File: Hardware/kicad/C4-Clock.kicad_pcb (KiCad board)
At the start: 2 copper layers, 99 x 99 mm, 29 parts, among them J1 Keypad, J2 Battery, J3 LCD1602, J4 Boost Module, J5 ICSP, K1 FINDER-36.11-5V, Q1 S9014, Q2 S9014, SW1 SW_SPST, SW2 SW_SPST, U1 ATmega328P-P, U2 AMS1117-5.0, U3 PCF8574A, U4 DS1302+, Y1 16MHz, Y2 32.768kHz

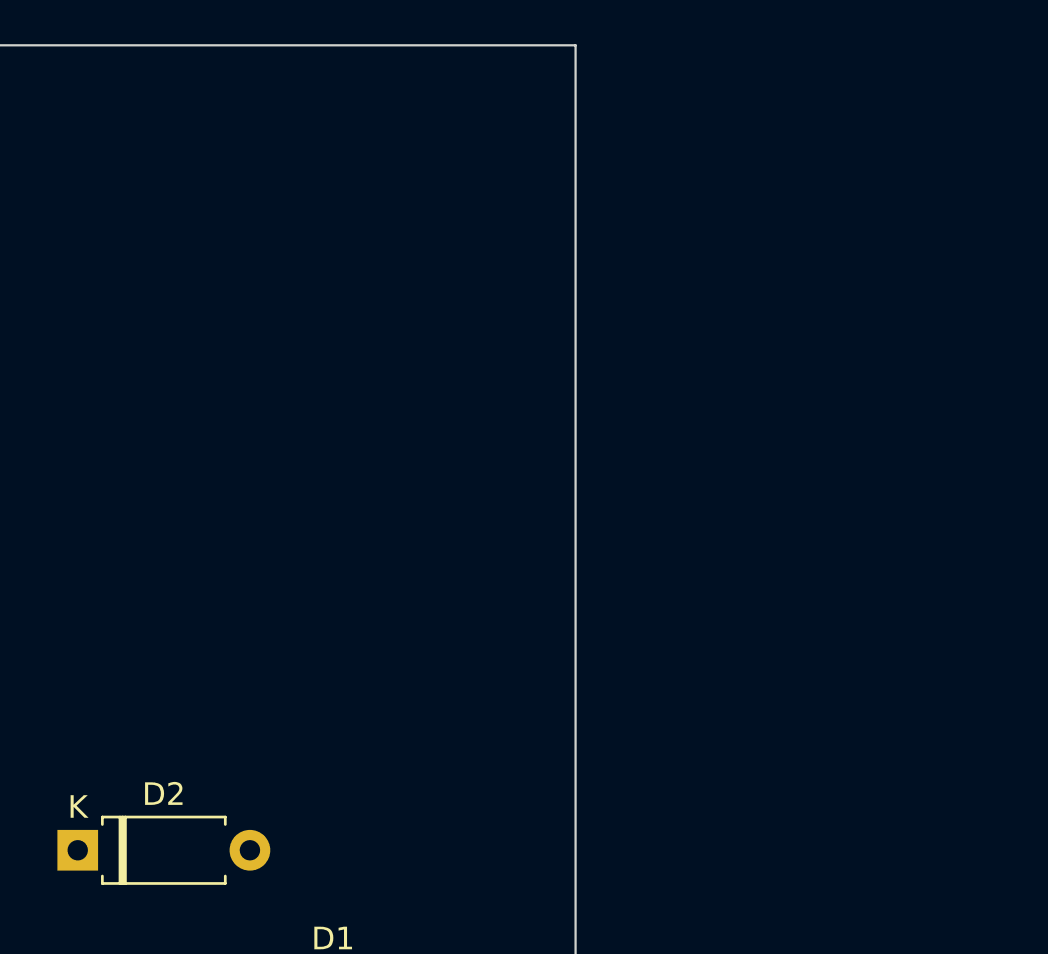
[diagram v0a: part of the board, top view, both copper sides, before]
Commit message: doc: Add lcd1602 reference
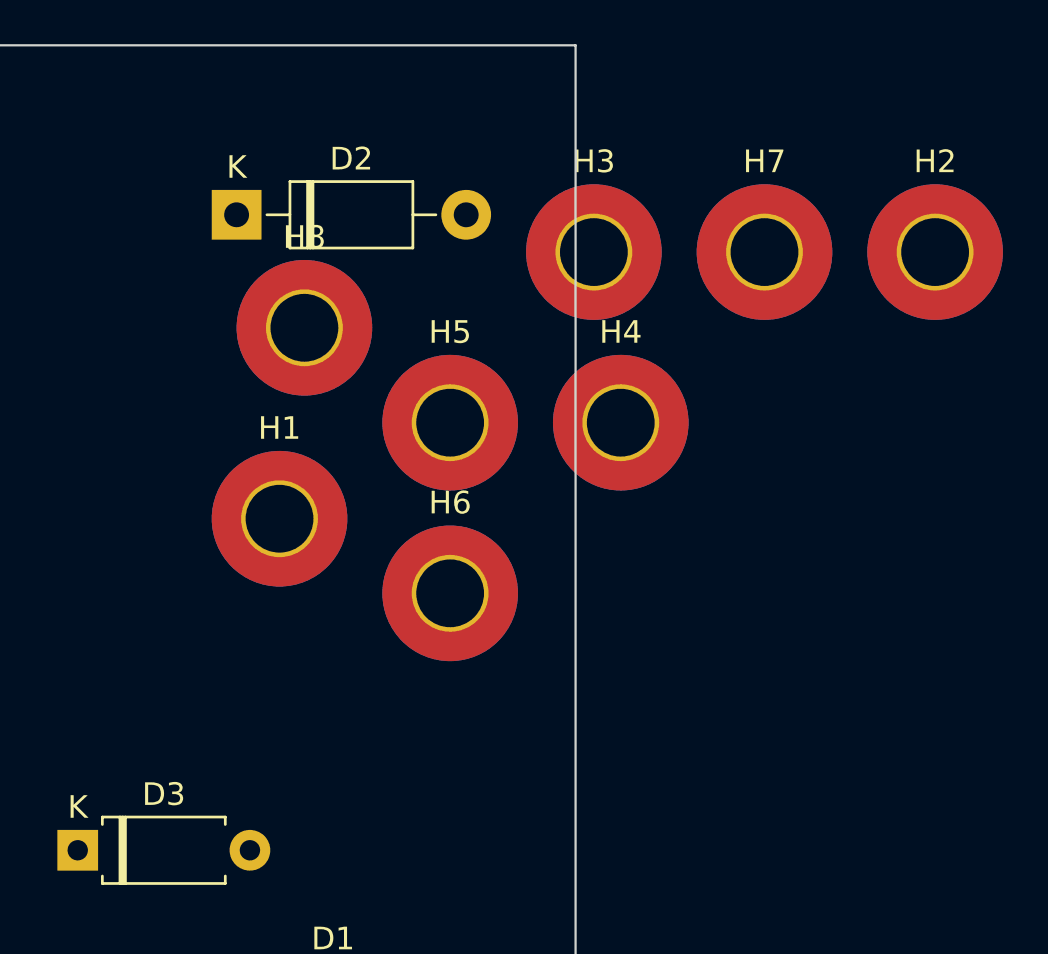
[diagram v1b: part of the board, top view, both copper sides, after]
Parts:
- added D2: 1N4001, Diode_THT:D_DO-41_SOD81_P10.16mm_Horizontal, F.Cu at (161.0, 47.0)
- added H1: LCD1602, MountingHole:MountingHole_3mm_Pad_TopBottom, F.Cu at (162.9, 60.5)
- added H2: hole, MountingHole:MountingHole_3mm_Pad_TopBottom, F.Cu at (191.9, 48.6)
- added H3: LCD1602, MountingHole:MountingHole_3mm_Pad_TopBottom, F.Cu at (176.8, 48.6)
- added H4: hole, MountingHole:MountingHole_3mm_Pad_TopBottom, F.Cu at (178.0, 56.2)
- added H5: LCD1602, MountingHole:MountingHole_3mm_Pad_TopBottom, F.Cu at (170.4, 56.2)
- added H6: hole, MountingHole:MountingHole_3mm_Pad_TopBottom, F.Cu at (170.4, 63.8)
- added H7: LCD1602, MountingHole:MountingHole_3mm_Pad_TopBottom, F.Cu at (184.4, 48.6)
- added H8: hole, MountingHole:MountingHole_3mm_Pad_TopBottom, F.Cu at (164.0, 52.0)
- renumbered D2 to D3
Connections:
- J2 pad 1: +8V -> Net-(D2-Pad1)

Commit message: software: Added VS files
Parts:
- D3: footprint Diode_THT:D_A-405_P7.62mm_Horizontal -> Diode_THT:D_DO-41_SOD81_P10.16mm_Horizontal
- Y2: moved to F.Cu
- moved H6 113.0 mm to (82.0, 134.0)
- moved H2 111.3 mm to (81.0, 58.0)
- moved H5 84.8 mm to (88.0, 76.0)
- moved H8 82.4 mm to (172.0, 134.0)
- moved H1 76.5 mm to (88.0, 45.0)
- moved D2 72.2 mm to (89.0, 53.0), turned to -90 degrees
- moved C1 40.9 mm to (119.0, 106.5), turned to 90 degrees
- moved H7 34.7 mm to (163.0, 76.0)
- moved C4 34.0 mm to (101.5, 66.0), turned to 180 degrees
- moved D3 30.3 mm to (158.9, 105.0)
- moved R2 30.1 mm to (132.9, 65.0)
- moved SW2 29.0 mm to (145.4, 84.9), turned to 180 degrees
- moved C2 24.5 mm to (125.0, 106.5), turned to 90 degrees
- moved R1 21.9 mm to (132.9, 69.0)
- moved K1 21.9 mm to (164.0, 111.0), turned to -90 degrees
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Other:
- board text added: "+"
- board text added: "-"

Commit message: hardware: Add parts
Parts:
- added Q3: S9014, Package_TO_SOT_THT:TO-92, F.Cu at (156.0, 67.0)
- added R5: 1k, Resistor_THT:R_Axial_DIN0207_L6.3mm_D2.5mm_P10.16mm_Horizontal, F.Cu at (155.6, 61.7)
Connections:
- D3 pad 1: RELAY -> Net-(D3-Pad1)
- K1 pad A1: RELAY -> Net-(D3-Pad1)
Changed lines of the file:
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@@
   (net 56 "Net-(U4-Pad3)")
   (net 57 "Net-(D2-Pad1)")
+  (net 58 "Net-(D3-Pad1)")
+  (net 59 "Net-(Q3-Pad2)")
   (footprint "Package_TO_SOT_THT:TO-92" (layer "F.Cu")
     (at 152 81 -90)
@@
       (net 33 "Net-(K1-Pad14)") (pintype "passive"))
     (pad "A1" thru_hole circle (at 2 6 270) (size 3 3) (drill 1.3) (layers *.Cu *.Mask)
-      (net 8 "RELAY") (pintype "passive"))
+      (net 58 "Net-(D3-Pad1)") (pintype "passive"))
     (pad "A2" thru_hole circle (at 2 -6 270) (size 3 3) (drill 1.3) (layers *.Cu *.Mask)
       (net 3 "GND") (pintype "passive"))
@@
     (fp_line (start 2.48 1.35) (end 7.68 1.35) (layer "F.Fab") (width 0.1))
     (pad "1" thru_hole rect (at 0 0) (size 2.2 2.2) (drill 1.1) (layers *.Cu *.Mask)
-      (net 8 "RELAY") (pinfunction "K") (pintype "passive"))
+      (net 58 "Net-(D3-Pad1)") (pinfunction "K") (pintype "passive"))
     (pad "2" thru_hole oval (at 10.16 0) (size 2.2 2.2) (drill 1.1) (layers *.Cu *.Mask)
       (net 3 "GND") (pinfunction "A") (pintype "passive"))
@@
     (pad "1" connect circle (at 0 0) (size 6 6) (layers "B.Cu" "B.Mask")
       (net 3 "GND") (pinfunction "1") (pintype "input"))
+  )
+  (footprint "Resistor_THT:R_Axial_DIN0207_L6.3mm_D2.5mm_P10.16mm_Horizontal" (layer "F.Cu")
+    (at 155.59 61.72)
+    (descr "Resistor, Axial_DIN0207 series, Axial, Horizontal, pin pitch=10.16mm, 0.25W = 1/4W, length*diameter=6.3*2.5mm^2, http://cdn-reichelt.de/documents/datenblatt/B400/1_4W%23YAG.pdf")
+    (tags "Resistor Axial_DIN0207 series Axial Horizontal pin pitch 10.16mm 0.25W = 1/4W length 6.3mm diameter 2.5mm")
+    (property "Sheetfile" "C4-Clock.kicad_sch")
+    (property "Sheetname" "")
+    (attr through_hole)
+    (fp_text reference "R5" (at 5.08 -2.37) (layer "F.SilkS")
+      (effects (font (size 1 1) (thickness 0.15)))
+    )
+    (fp_text value "1k" (at 5.08 2.37) (layer "F.Fab")
+      (effects (font (size 1 1) (thickness 0.15)))
+    )
+    (fp_text user "${REFERENCE}" (at 5.08 0) (layer "F.Fab")
+      (effects (font (size 1 1) (thickness 0.15)))
+    )
+    (fp_line (start 8.35 1.37) (end 8.35 -1.37) (layer "F.SilkS") (width 0.12))
+    (fp_line (start 1.81 1.37) (end 8.35 1.37) (layer "F.SilkS") (width 0.12))
+    (fp_line (start 1.04 0) (end 1.81 0) (layer "F.SilkS") (width 0.12))
+    (fp_line (start 9.12 0) (end 8.35 0) (layer "F.SilkS") (width 0.12))
+    (fp_line (start 8.35 -1.37) (end 1.81 -1.37) (layer "F.SilkS") (width 0.12))
+    (fp_line (start 1.81 -1.37) (end 1.81 1.37) (layer "F.SilkS") (width 0.12))
+    (fp_line (start -1.05 -1.5) (end -1.05 1.5) (layer "F.CrtYd") (width 0.05))
+    (fp_line (start 11.21 1.5) (end 11.21 -1.5) (layer "F.CrtYd") (width 0.05))
+    (fp_line (start 11.21 -1.5) (end -1.05 -1.5) (layer "F.CrtYd") (width 0.05))
+    (fp_line (start -1.05 1.5) (end 11.21 1.5) (layer "F.CrtYd") (width 0.05))
+    (fp_line (start 1.93 -1.25) (end 1.93 1.25) (layer "F.Fab") (width 0.1))
+    (fp_line (start 1.93 1.25) (end 8.23 1.25) (layer "F.Fab") (width 0.1))
+    (fp_line (start 8.23 1.25) (end 8.23 -1.25) (layer "F.Fab") (width 0.1))
+    (fp_line (start 0 0) (end 1.93 0) (layer "F.Fab") (width 0.1))
+    (fp_line (start 8.23 -1.25) (end 1.93 -1.25) (layer "F.Fab") (width 0.1))
+    (fp_line (start 10.16 0) (end 8.23 0) (layer "F.Fab") (width 0.1))
+    (pad "1" thru_hole circle (at 0 0) (size 1.6 1.6) (drill 0.8) (layers *.Cu *.Mask)
+      (net 8 "RELAY") (pintype "passive"))
+    (pad "2" thru_hole oval (at 10.16 0) (size 1.6 1.6) (drill 0.8) (layers *.Cu *.Mask)
+      (net 59 "Net-(Q3-Pad2)") (pintype "passive"))
+    (model "${KICAD6_3DMODEL_DIR}/Resistor_THT.3dshapes/R_Axial_DIN0207_L6.3mm_D2.5mm_P10.16mm_Horizontal.wrl"
+      (offset (xyz 0 0 0))
+      (scale (xyz 1 1 1))
+      (rotate (xyz 0 0 0))
+    )
   )
   (footprint "Resistor_THT:R_Axial_DIN0207_L6.3mm_D2.5mm_P10.16mm_Horizontal" (layer "F.Cu")
@@
       (offset (xyz 0 0 0))
       (scale (xyz 1 1 1))
+      (rotate (xyz 0 0 0))
+    )
+  )
+  (footprint "Package_TO_SOT_THT:TO-92" (layer "F.Cu")
+    (at 156 67)
+    (descr "TO-92 leads molded, narrow, drill 0.75mm (see NXP sot054_po.pdf)")
+    (tags "to-92 sc-43 sc-43a sot54 PA33 transistor")
+    (property "Sheetfile" "C4-Clock.kicad_sch")
+    (property "Sheetname" "")
+    (attr through_hole)
+    (fp_text reference "Q3" (at 1.27 -3.56) (layer "F.SilkS")
+      (effects (font (size 1 1) (thickness 0.15)))
+    )
+    (fp_text value "S9014" (at 1.27 2.79) (layer "F.Fab")
+      (effects (font (size 1 1) (thickness 0.15)))
+    )
+    (fp_text user "${REFERENCE}" (at 1.27 0) (layer "F.Fab")
+      (effects (font (size 1 1) (thickness 0.15)))
+    )
+    (fp_line (start -0.53 1.85) (end 3.07 1.85) (layer "F.SilkS") (width 0.12))
+    (fp_arc (start 1.27 -2.6) (mid 3.672087 -0.994977) (end 3.108478 1.838478) (layer "F.SilkS") (width 0.12))
+    (fp_arc (start -0.568478 1.838478) (mid -1.132087 -0.994977) (end 1.27 -2.6) (layer "F.SilkS") (width 0.12))
+    (fp_line (start -1.46 -2.73) (end -1.46 2.01) (layer "F.CrtYd") (width 0.05))
+    (fp_line (start 4 2.01) (end 4 -2.73) (layer "F.CrtYd") (width 0.05))
+    (fp_line (start -1.46 -2.73) (end 4 -2.73) (layer "F.CrtYd") (width 0.05))
+    (fp_line (start 4 2.01) (end -1.46 2.01) (layer "F.CrtYd") (width 0.05))
+    (fp_line (start -0.5 1.75) (end 3 1.75) (layer "F.Fab") (width 0.1))
+    (fp_arc (start -0.483625 1.753625) (mid -1.021221 -0.949055) (end 1.27 -2.48) (layer "F.Fab") (width 0.1))
+    (fp_arc (start 1.27 -2.48) (mid 3.561221 -0.949055) (end 3.023625 1.753625) (layer "F.Fab") (width 0.1))
+    (pad "1" thru_hole rect (at 0 0) (size 1.3 1.3) (drill 0.75) (layers *.Cu *.Mask)
+      (net 58 "Net-(D3-Pad1)") (pinfunction "E") (pintype "passive"))
+    (pad "2" thru_hole circle (at 1.27 -1.27) (size 1.3 1.3) (drill 0.75) (layers *.Cu *.Mask)
+      (net 59 "Net-(Q3-Pad2)") (pinfunction "B") (pintype "passive"))
+    (pad "3" thru_hole circle (at 2.54 0) (size 1.3 1.3) (drill 0.75) (layers *.Cu *.Mask)
+      (net 1 "+5V") (pinfunction "C") (pintype "passive"))
+    (model "${KICAD6_3DMODEL_DIR}/Package_TO_SOT_THT.3dshapes/TO-92.wrl"
+      (offset (xyz 0 0 0))
+      (scale (xyz 1 1 1))

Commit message: hardware: Update PCB
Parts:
- removed C5: 0.1uF, Capacitor_THT:C_Disc_D3.0mm_W1.6mm_P2.50mm
- U4: footprint Package_DIP:DIP-8_W7.62mm -> Package_DIP:DIP-8_W7.62mm_Socket
- moved R5 26.3 mm to (132.9, 75.0)
- moved C4 21.4 mm to (88.5, 83.0)
- moved H8 16.0 mm to (156.0, 134.0)
- moved D2 10.1 mm to (89.0, 63.1), turned to 90 degrees
- moved D1 6.71 mm to (164.0, 86.0)
- moved BZ1 6.32 mm to (162.2, 99.0)
- moved K1 5.83 mm to (167.0, 116.0)
- moved D3 5.39 mm to (160.9, 110.0)
- moved SW1 2.83 mm to (83.6, 65.6)
- moved J2 2.00 mm to (79.0, 51.0)
- moved J5 2.00 mm to (87.3, 94.5)
- moved R1 2.00 mm to (132.9, 67.0)
- moved R2 2.00 mm to (132.9, 63.0)
- moved R4 2.00 mm to (132.9, 71.0)
- moved H2 1.00 mm to (82.0, 58.0)
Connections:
- D2 pad 1: Net-(D2-Pad1) -> +8V
- D2 pad 2: +8V -> Net-(D2-Pad2)
- J2 pad 1: Net-(D2-Pad1) -> Net-(D2-Pad2)
- U1 pad 25: unconnected-(U1-Pad25) -> DS1302_CLK
- U1 pad 26: unconnected-(U1-Pad26) -> DS1302_IO
- U4 pad 5: PB5 -> PB3
- U4 pad 6: PB4 -> DS1302_IO
- U4 pad 7: PB3 -> DS1302_CLK
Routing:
- net GND: track 0.00 -> 162.1 mm
- net +5V: track 0.00 -> 111.8 mm, vias 0 -> 4
- net PB3: track 0.00 -> 100.5 mm, vias 0 -> 1
- net Net-(C3-Pad2): track 0.00 -> 74.1 mm
- net Net-(D3-Pad1): track 0.00 -> 53.0 mm
- net Net-(J1-Pad8): track 0.00 -> 52.5 mm
- net Net-(K1-Pad14): track 0.00 -> 51.7 mm
- net DS1302_CLK: track 0.00 -> 50.6 mm
- net DS1302_IO: track 0.00 -> 50.0 mm
- net Net-(J1-Pad1): track 0.00 -> 48.6 mm
- net Net-(J1-Pad2): track 0.00 -> 48.3 mm
- net Net-(J1-Pad3): track 0.00 -> 48.0 mm
- net Net-(J1-Pad4): track 0.00 -> 46.9 mm
- net Net-(J1-Pad5): track 0.00 -> 46.4 mm
- net Net-(Q2-Pad2): track 0.00 -> 46.1 mm, vias 0 -> 1
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- added copper zone on F.Cu, net +5V
- added copper zone on B.Cu, net GND
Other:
- board text added: "C3"
- board text added: "C4 Clock by yangshunhuai https://github.com/yangshunhuai/C4-Clock"
